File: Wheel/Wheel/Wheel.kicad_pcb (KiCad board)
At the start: 2 copper layers, 162 x 112 mm, 142 parts, among them J1 Conn_02x09_Odd_Even, J10 RJ45, J11 Screw_Terminal_01x02, J12 DS-201, J13 Conn_01x04, J14 Conn_02x13_Top_Bottom, J15 DB25_Female, J16 Conn_01x06, J17 Conn_01x07, J18 Conn_01x06, J19 RJ45, J2 RJ45, J20 DB9_Male, J21 DB9_Female, J22 Conn_02x15_Odd_Even, J3 RJ45, J4 RJ45, J5 USB_B, J6 Conn_02x10_Odd_Even, J7 Conn_02x09_Odd_Even, J8 RJ45, J9 RJ45, U1 MCP23S17_SP, U10 PC817, U11 IP4220CZ6, U12 IP4220CZ6, U13 IP4220CZ6, U14 IP4220CZ6, U15 IP4220CZ6, U16 IP4220CZ6, U17 IP4220CZ6, U18 IP4220CZ6, U19 IP4220CZ6, U2 STM32F407VETx, U20 IP4220CZ6, U21 PC817, U3 MCP23S17_SP, U4 USBLC6-2SC6, U5 AMS1117, U6 4N35, U7 PC817, U8 PC817, U9 PC817, Y1 32,768 кГц, Y2 8MHz

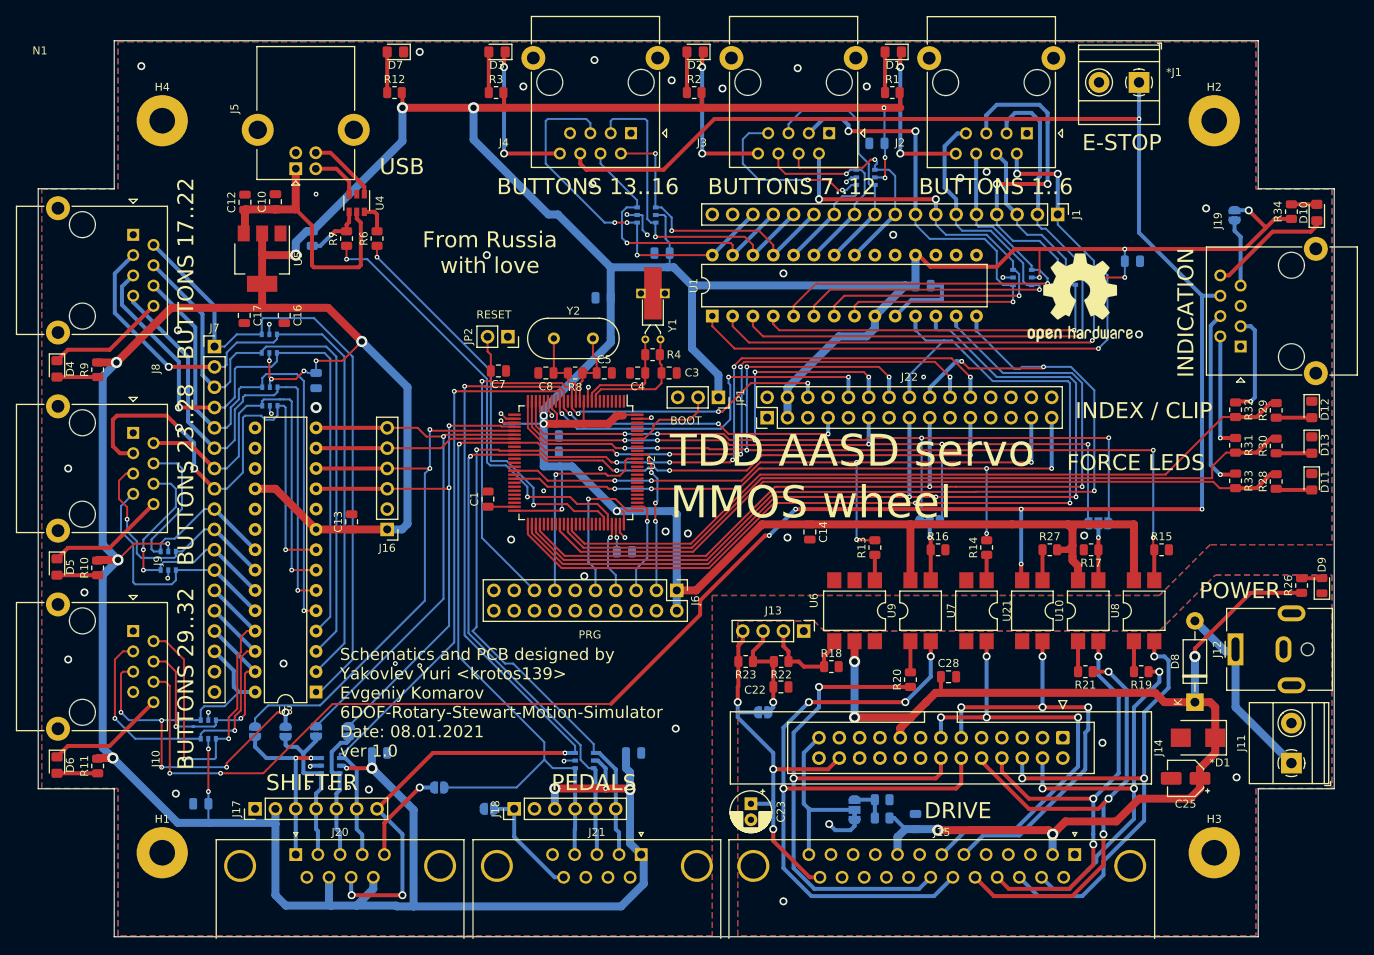
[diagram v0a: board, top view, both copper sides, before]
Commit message: I've changed wheel's PCB, I've added GERBER files
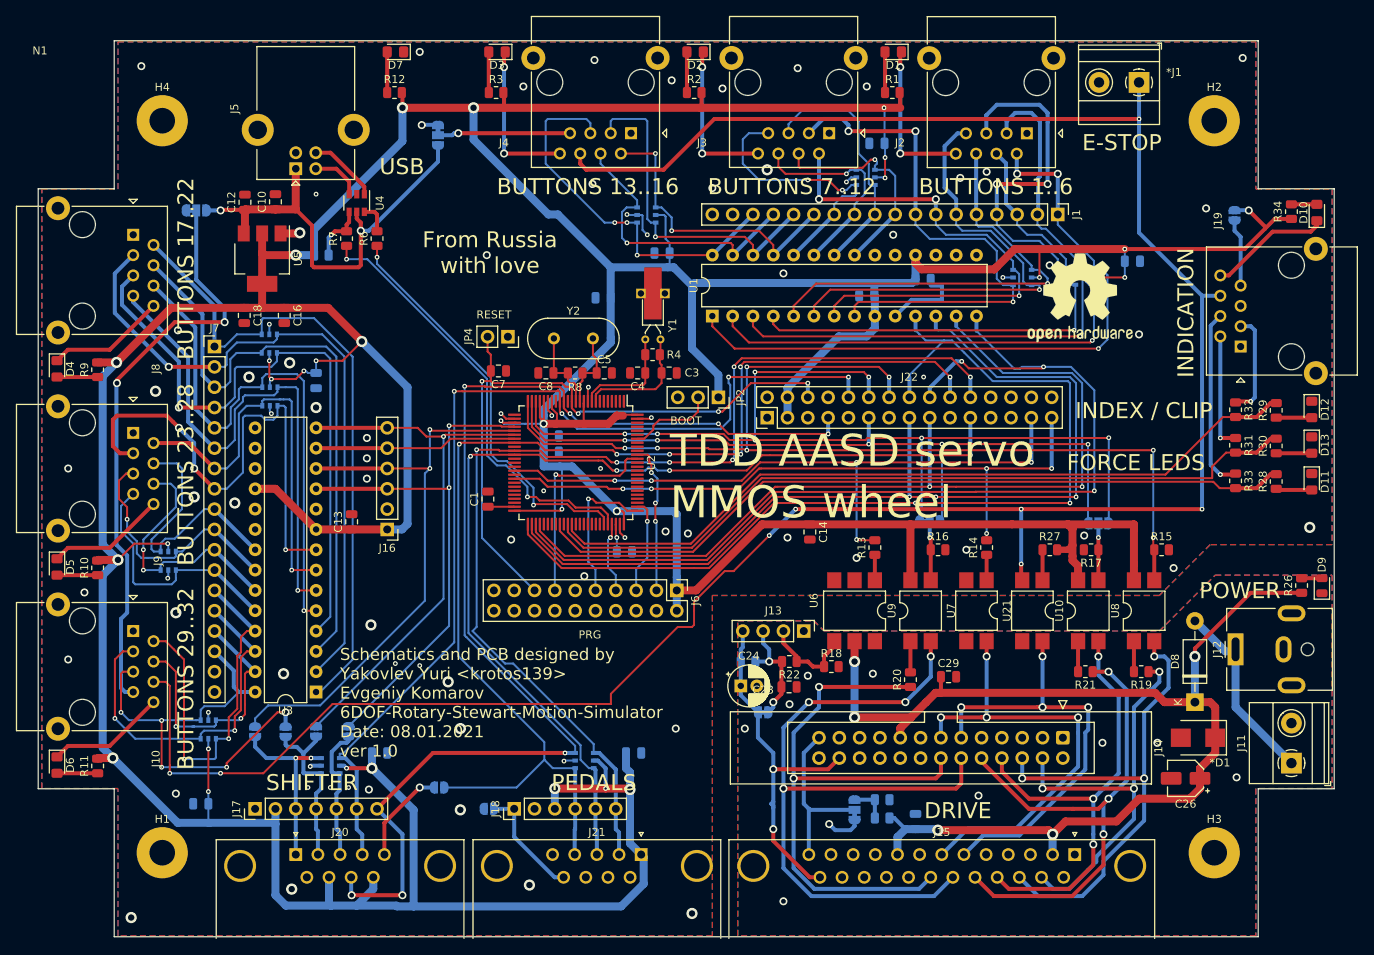
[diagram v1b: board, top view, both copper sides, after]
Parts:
- removed the C23 at (119.1, 119.4)
- added C17: 104, Capacitor_SMD:C_0805_2012Metric, B.Cu at (133.6, 55.9)
- added C24: 1uF, Capacitor_THT:CP_Radial_D5.0mm_P2.00mm, F.Cu at (117.9, 104.6)
- added JP1: SolderJumper_3_Bridged12, Jumper:SolderJumper-3_P1.3mm_Bridged12_RoundedPad1.0x1.5mm, B.Cu at (80.0, 35.8)
- added JP3: SolderJumper_3_Bridged12, Jumper:SolderJumper-3_P1.3mm_Bridged12_RoundedPad1.0x1.5mm, B.Cu at (49.8, 45.2)
- R23: moved to B.Cu
- moved R5 2.36 mm to (65.4, 50.8), turned to 0 degrees
- moved C23 1.02 mm to (123.9, 104.8)
- moved R22 1.02 mm to (123.9, 101.6)
- moved C11 0.76 mm to (140.7, 53.8)
- moved R23 0.30 mm to (118.8, 101.6)
- renumbered C17 to C18, C18 to C19, C19 to C20, C20 to C21, C21 to C22, C22 to C23, C24 to C25, C25 to C26, C26 to C27, C27 to C28, C28 to C29, C29 to C30, JP8 to JP10, JP9 to JP11, JP10 to JP12, JP11 to JP13, JP12 to JP14, JP13 to JP15, JP1 to JP2, JP2 to JP4, JP3 to JP5, JP4 to JP6, JP5 to JP7, JP6 to JP8, JP7 to JP9
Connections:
- J10 pad 7: GND -> Net-(J10-Pad7)
- J4 pad 7: GND -> Net-(J4-Pad7)
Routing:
- net Net-(J10-Pad7): track 0.00 -> 73.0 mm, vias 0 -> 2
- net 5V: track 35.5 -> 55.6 mm, vias 0 -> 2
- net 3V: track 818.9 -> 838.5 mm, vias 32 -> 31
- net Net-(J4-Pad7): track 0.00 -> 16.6 mm, vias 0 -> 1
- net DRIVE_VREF: track 50.9 -> 45.7 mm, vias 3 -> 2
- net GND: track 35.1 -> 39.6 mm, vias 56 -> 83
- net DRIVE_ENABLE: track 298.8 -> 300.2 mm
- net Net-(C23-Pad1): track 13.6 -> 14.5 mm, vias 1 -> 2
- net Net-(J13-Pad2): track 12.5 -> 11.9 mm
- net COM: vias 4 -> 10
